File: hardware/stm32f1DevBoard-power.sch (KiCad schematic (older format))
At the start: 17 parts, among them J2 POWER_JACK, Q1 MOSFET-N, U3 LM358, U4 VREG_GNDCENTER, U5 VREG_VOUTCENTER

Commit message: more mods
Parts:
- added unit 2 of U3
- D2: value POWER -> POWERLED
- JP8: value JUMPER_3X1 -> BATTERYENABLE
- U4: value VREG_GNDCENTER -> VREG-X-5
- U5: value VREG_VOUTCENTER -> VREG-5-3.3
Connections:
- wire segments 55 -> 62
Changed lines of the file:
@@
-EESchema Schematic File Version 2  date Sun 16 Dec 2012 03:06:52 PM EST
+EESchema Schematic File Version 2  date Sun 16 Dec 2012 11:20:27 PM EST
 LIBS:stm32f1DevBoard
 LIBS:power
@@
 Sheet 3 4
 Title ""
-Date "16 dec 2012"
+Date "17 dec 2012"
 Rev ""
 Comp ""
@@
 P 3250 1450
 F 0 "JP8" H 3200 1600 60  0000 C CNN
-F 1 "JUMPER_3X1" H 3250 1250 60  0000 C CNN
+F 1 "BATTERYENABLE" H 3250 1250 60  0000 C CNN
 	1    3250 1450
 	1    0    0    -1
@@
 L MOSFET-N Q1
 U 1 1 50CE2C67
-P 4150 6150
-F 0 "Q1" H 4200 6300 60  0000 C CNN
-F 1 "MOSFET-N" H 4400 6000 60  0000 C CNN
-	1    4150 6150
+P 5650 6250
+F 0 "Q1" H 5700 6400 60  0000 C CNN
+F 1 "MOSFET-N" H 5900 6100 60  0000 C CNN
+	1    5650 6250
 	1    0    0    -1
 $EndComp
@@
 L +5V #PWR048
 U 1 1 50CE2C6E
-P 4400 6150
-F 0 "#PWR048" H 4400 6240 20  0001 C CNN
-F 1 "+5V" H 4400 6240 30  0000 C CNN
-	1    4400 6150
+P 5900 6250
+F 0 "#PWR048" H 5900 6340 20  0001 C CNN
+F 1 "+5V" H 5900 6340 30  0000 C CNN
+	1    5900 6250
 	1    0    0    -1
 $EndComp
@@
 P 3700 3700
 F 0 "U4" H 3850 3504 60  0000 C CNN
-F 1 "VREG_GNDCENTER" H 3700 3900 60  0000 C CNN
+F 1 "VREG-X-5" H 3700 3900 60  0000 C CNN
 	1    3700 3700
 	1    0    0    -1
@@
 P 8150 3800
 F 0 "U5" H 8300 3604 60  0000 C CNN
-F 1 "VREG_VOUTCENTER" H 8150 4000 60  0000 C CNN
+F 1 "VREG-5-3.3" H 8150 4000 60  0000 C CNN
 	1    8150 3800
 	1    0    0    -1
@@
 	3200 5700 3200 5750
 Wire Wire Line
-	3800 6150 3900 6150
-Wire Wire Line
-	4100 5950 4100 5750
-Wire Wire Line
-	4100 5750 4000 5750
-Wire Wire Line
-	4400 6150 4400 6450
-Wire Wire Line
-	4100 6450 4100 6350
+	5600 6050 5600 5850
+Wire Wire Line
+	5600 5850 5500 5850
+Wire Wire Line
+	5900 6250 5900 6550
+Wire Wire Line
+	5600 6550 5600 6450
 Wire Wire Line
 	8150 4050 8150 4100
 Wire Wire Line
-	4400 6450 4100 6450
+	5900 6550 5600 6550
 Wire Wire Line
 	8550 3750 8850 3750
@@
 P 8550 1600
 F 0 "D2" H 8550 1700 50  0000 C CNN
-F 1 "POWER" H 8550 1500 50  0000 C CNN
+F 1 "POWERLED" H 8550 1500 50  0000 C CNN
 	1    8550 1600
 	1    0    0    -1
@@
 Text GLabel 3650 1450 2    60   Input ~ 0
 VBAT
-Text GLabel 4000 5750 0    60   Input ~ 0
+Text GLabel 5500 5850 0    60   Input ~ 0
 VUSB
 Text GLabel 2200 5500 0    60   Input ~ 0
@@
 Text GLabel 3250 3650 0    60   Input ~ 0
 VIN
+$Comp
+L LM358 U3
+U 2 1 50CE9E50
+P 4500 6250
+F 0 "U3" H 4450 6450 60  0000 L CNN
+F 1 "LM358" H 4450 6000 60  0000 L CNN
+	2    4500 6250
+	1    0    0    -1
+$EndComp
+Wire Wire Line
+	3800 6150 4000 6150
+Wire Wire Line
+	5000 6250 5400 6250
+Wire Wire Line
+	5100 6250 5100 6850
+Wire Wire Line
+	5100 6850 3900 6850
+Wire Wire Line
+	3900 6850 3900 6350
+Wire Wire Line
+	3900 6350 4000 6350
+Connection ~ 5100 6250
+$Comp
+L GND #PWR?
+U 1 1 50CEA124
+P 4400 6700
+F 0 "#PWR?" H 4400 6700 30  0001 C CNN
+F 1 "GND" H 4400 6630 30  0001 C CNN
+	1    4400 6700
+	1    0    0    -1
+$EndComp
+$Comp
+L +5V #PWR?
+U 1 1 50CEA12A
+P 4400 5800
+F 0 "#PWR?" H 4400 5890 20  0001 C CNN
+F 1 "+5V" H 4400 5890 30  0000 C CNN
+	1    4400 5800
+	1    0    0    -1
+$EndComp
+Wire Wire Line
+	4400 6650 4400 6700
+Wire Wire Line
+	4400 5800 4400 5850
 $EndSCHEMATC

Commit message: changed to p-ch mosfet
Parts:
- removed Q1: MOSFET-N, symbol MOSFET-N
- added Q1: MOSFET-P, symbol MOSFET-P
- R14: value ? -> 68k
- R15: value ? -> 33k
- R16, R17: value ? -> 100k
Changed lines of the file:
@@
-EESchema Schematic File Version 2  date Wed 19 Dec 2012 08:51:07 PM EST
+EESchema Schematic File Version 2  date Wed 19 Dec 2012 11:05:56 PM EST
 LIBS:stm32f1DevBoard
 LIBS:power
@@
 Sheet 3 4
 Title ""
-Date "19 dec 2012"
+Date "20 dec 2012"
 Rev ""
 Comp ""
@@
 $EndComp
 $Comp
-L GND #PWR38
+L GND #PWR038
 U 1 1 50CE2BF2
 P 2100 1800
-F 0 "#PWR38" H 2100 1800 30  0001 C CNN
+F 0 "#PWR038" H 2100 1800 30  0001 C CNN
 F 1 "GND" H 2100 1730 30  0001 C CNN
 	1    2100 1800
@@
 $EndComp
 $Comp
-L +3.3V #PWR42
+L +3.3V #PWR039
 U 1 1 50CE2BF8
 P 2900 1300
-F 0 "#PWR42" H 2900 1260 30  0001 C CNN
+F 0 "#PWR039" H 2900 1260 30  0001 C CNN
 F 1 "+3.3V" H 2900 1410 30  0000 C CNN
 	1    2900 1300
@@
 $EndComp
 $Comp
-L GND #PWR40
+L GND #PWR040
 U 1 1 50CE2C12
 P 2600 3950
-F 0 "#PWR40" H 2600 3950 30  0001 C CNN
+F 0 "#PWR040" H 2600 3950 30  0001 C CNN
 F 1 "GND" H 2600 3880 30  0001 C CNN
 	1    2600 3950
@@
 $EndComp
 $Comp
-L GND #PWR45
+L GND #PWR041
 U 1 1 50CE2C18
 P 3600 4050
-F 0 "#PWR45" H 3600 4050 30  0001 C CNN
+F 0 "#PWR041" H 3600 4050 30  0001 C CNN
 F 1 "GND" H 3600 3980 30  0001 C CNN
 	1    3600 4050
@@
 $EndComp
 $Comp
-L +5V #PWR49
+L +5V #PWR042
 U 1 1 50CE2C1E
 P 4500 3550
-F 0 "#PWR49" H 4500 3640 20  0001 C CNN
+F 0 "#PWR042" H 4500 3640 20  0001 C CNN
 F 1 "+5V" H 4500 3640 30  0000 C CNN
 	1    4500 3550
@@
 $EndComp
 $Comp
-L GND #PWR46
+L GND #PWR043
 U 1 1 50CE2C2A
 P 4200 4050
-F 0 "#PWR46" H 4200 4050 30  0001 C CNN
+F 0 "#PWR043" H 4200 4050 30  0001 C CNN
 F 1 "GND" H 4200 3980 30  0001 C CNN
 	1    4200 4050
@@
 P 2700 5800
 F 0 "R16" H 2710 5890 60  0000 C CNN
-F 1 "?" H 2710 5700 60  0000 C CNN
+F 1 "100k" H 2710 5700 60  0000 C CNN
 	1    2700 5800
 	0    -1   -1   0
@@
 P 2700 6550
 F 0 "R17" H 2710 6640 60  0000 C CNN
-F 1 "?" H 2710 6450 60  0000 C CNN
+F 1 "100k" H 2710 6450 60  0000 C CNN
 	1    2700 6550
 	0    -1   -1   0
@@
 P 2400 5800
 F 0 "R14" H 2410 5890 60  0000 C CNN
-F 1 "?" H 2410 5700 60  0000 C CNN
+F 1 "68k" H 2410 5700 60  0000 C CNN
 	1    2400 5800
 	0    -1   -1   0
@@
 P 2400 6550
 F 0 "R15" H 2410 6640 60  0000 C CNN
-F 1 "?" H 2410 6450 60  0000 C CNN
+F 1 "33k" H 2410 6450 60  0000 C CNN
 	1    2400 6550
 	0    -1   -1   0
 $EndComp
 $Comp
-L +5V #PWR41
+L +5V #PWR044
 U 1 1 50CE2C4E
 P 2700 5550
-F 0 "#PWR41" H 2700 5640 20  0001 C CNN
+F 0 "#PWR044" H 2700 5640 20  0001 C CNN
 F 1 "+5V" H 2700 5640 30  0000 C CNN
 	1    2700 5550
@@
 $EndComp
 $Comp
-L GND #PWR39
+L GND #PWR045
 U 1 1 50CE2C55
 P 2400 6800
-F 0 "#PWR39" H 2400 6800 30  0001 C CNN
+F 0 "#PWR045" H 2400 6800 30  0001 C CNN
 F 1 "GND" H 2400 6730 30  0001 C CNN
 	1    2400 6800
@@
 $EndComp
 $Comp
-L GND #PWR44
+L GND #PWR046
 U 1 1 50CE2C5B
 P 3200 6600
-F 0 "#PWR44" H 3200 6600 30  0001 C CNN
+F 0 "#PWR046" H 3200 6600 30  0001 C CNN
 F 1 "GND" H 3200 6530 30  0001 C CNN
 	1    3200 6600
@@
 $EndComp
 $Comp
-L +5V #PWR43
+L +5V #PWR047
 U 1 1 50CE2C61
 P 3200 5700
-F 0 "#PWR43" H 3200 5790 20  0001 C CNN
+F 0 "#PWR047" H 3200 5790 20  0001 C CNN
 F 1 "+5V" H 3200 5790 30  0000 C CNN
 	1    3200 5700
@@
 $EndComp
 $Comp
-L MOSFET-N Q1
-U 1 1 50CE2C67
-P 5650 6250
-F 0 "Q1" H 5700 6400 60  0000 C CNN
-F 1 "MOSFET-N" H 5900 6100 60  0000 C CNN
-	1    5650 6250
-	1    0    0    -1
-$EndComp
-$Comp
-L +5V #PWR50
+L +5V #PWR048
 U 1 1 50CE2C6E
 P 5900 6250
-F 0 "#PWR50" H 5900 6340 20  0001 C CNN
+F 0 "#PWR048" H 5900 6340 20  0001 C CNN
 F 1 "+5V" H 5900 6340 30  0000 C CNN
 	1    5900 6250
@@
 $EndComp
 $Comp
-L GND #PWR53
+L GND #PWR049
 U 1 1 50CE2C74
 P 8150 4100
-F 0 "#PWR53" H 8150 4100 30  0001 C CNN
+F 0 "#PWR049" H 8150 4100 30  0001 C CNN
 F 1 "GND" H 8150 4030 30  0001 C CNN
 	1    8150 4100
@@
 $EndComp
 $Comp
-L +3.3V #PWR56
+L +3.3V #PWR050
 U 1 1 50CE2C7A
 P 8850 3650
-F 0 "#PWR56" H 8850 3610 30  0001 C CNN
+F 0 "#PWR050" H 8850 3610 30  0001 C CNN
 F 1 "+3.3V" H 8850 3760 30  0000 C CNN
 	1    8850 3650
@@
 $EndComp
 $Comp
-L GND #PWR54
+L GND #PWR051
 U 1 1 50CE2C86
 P 8750 4200
-F 0 "#PWR54" H 8750 4200 30  0001 C CNN
+F 0 "#PWR051" H 8750 4200 30  0001 C CNN
 F 1 "GND" H 8750 4130 30  0001 C CNN
 	1    8750 4200
@@
 $EndComp
 $Comp
-L +5V #PWR51
+L +5V #PWR052
 U 1 1 50CE2C8C
 P 7650 3600
-F 0 "#PWR51" H 7650 3690 20  0001 C CNN
+F 0 "#PWR052" H 7650 3690 20  0001 C CNN
 F 1 "+5V" H 7650 3690 30  0000 C CNN
 	1    7650 3600
@@
 $EndComp
 $Comp
-L GND #PWR55
+L GND #PWR053
 U 1 1 50CE2CF6
 P 8850 1700
-F 0 "#PWR55" H 8850 1700 30  0001 C CNN
+F 0 "#PWR053" H 8850 1700 30  0001 C CNN
 F 1 "GND" H 8850 1630 30  0001 C CNN
 	1    8850 1700
@@
 	8350 1600 8200 1600
 $Comp
-L +3.3V #PWR52
+L +3.3V #PWR054
 U 1 1 50CE2CFF
 P 7750 1500
-F 0 "#PWR52" H 7750 1460 30  0001 C CNN
+F 0 "#PWR054" H 7750 1460 30  0001 C CNN
 F 1 "+3.3V" H 7750 1610 30  0000 C CNN
 	1    7750 1500
@@
 Connection ~ 5100 6250
 $Comp
-L GND #PWR48
+L GND #PWR055
 U 1 1 50CEA124
 P 4400 6700
-F 0 "#PWR48" H 4400 6700 30  0001 C CNN
+F 0 "#PWR055" H 4400 6700 30  0001 C CNN
 F 1 "GND" H 4400 6630 30  0001 C CNN
 	1    4400 6700
@@
 $EndComp
 $Comp
-L +5V #PWR47
+L +5V #PWR056
 U 1 1 50CEA12A
 P 4400 5800
-F 0 "#PWR47" H 4400 5890 20  0001 C CNN
+F 0 "#PWR056" H 4400 5890 20  0001 C CNN
 F 1 "+5V" H 4400 5890 30  0000 C CNN
 	1    4400 5800
@@
 Wire Wire Line
 	4400 5800 4400 5850
+$Comp
+L MOSFET-P Q1
+U 1 1 50D29082
+P 5650 6250
+F 0 "Q1" H 5700 6400 60  0000 C CNN
+F 1 "MOSFET-P" H 5900 6100 60  0000 C CNN
+	1    5650 6250
+	1    0    0    -1
+$EndComp
 $EndSCHEMATC

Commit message: using kicadcloud files
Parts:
- C15, C16: symbol CSMALL -> CPsmall
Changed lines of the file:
@@
-EESchema Schematic File Version 2  date Wed 19 Dec 2012 11:05:56 PM EST
-LIBS:stm32f1DevBoard
+EESchema Schematic File Version 2  date Wed 02 Jan 2013 12:15:05 PM EST
+LIBS:userFavorites
 LIBS:power
-LIBS:device
-LIBS:transistors
-LIBS:conn
-LIBS:linear
-LIBS:regul
-LIBS:74xx
-LIBS:cmos4000
-LIBS:adc-dac
-LIBS:memory
-LIBS:xilinx
-LIBS:special
-LIBS:microcontrollers
-LIBS:dsp
-LIBS:microchip
-LIBS:analog_switches
-LIBS:motorola
-LIBS:texas
-LIBS:intel
-LIBS:audio
-LIBS:interface
-LIBS:digital-audio
-LIBS:philips
-LIBS:display
-LIBS:cypress
-LIBS:siliconi
-LIBS:opto
-LIBS:atmel
-LIBS:contrib
-LIBS:valves
-LIBS:stm32f1DevBoard-cache
 EELAYER 27 0
 EELAYER END
@@
 $EndComp
 $Comp
-L CSMALL C15
+L CPsmall C15
 U 1 1 50CE2C24
 P 4400 3850
@@
 $EndComp
 $Comp
-L CSMALL C16
+L CPsmall C16
 U 1 1 50CE2C80
 P 8750 4050

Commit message: updates to schematic
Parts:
- R18: value ? -> 100
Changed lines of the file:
@@
-EESchema Schematic File Version 2  date Thu 17 Jan 2013 09:41:47 PM EST
+EESchema Schematic File Version 2  date Mon 21 Jan 2013 10:28:50 PM EST
 LIBS:userFavorites
 LIBS:power
+LIBS:stm32f1DevBoard-cache
 EELAYER 27 0
 EELAYER END
@@
 Sheet 3 4
 Title ""
-Date "18 jan 2013"
+Date "22 jan 2013"
 Rev ""
 Comp ""
@@
 P 8000 1600
 F 0 "R18" H 8010 1690 60  0000 C CNN
-F 1 "?" H 8010 1500 60  0000 C CNN
+F 1 "100" H 8010 1500 60  0000 C CNN
 	1    8000 1600
 	1    0    0    -1

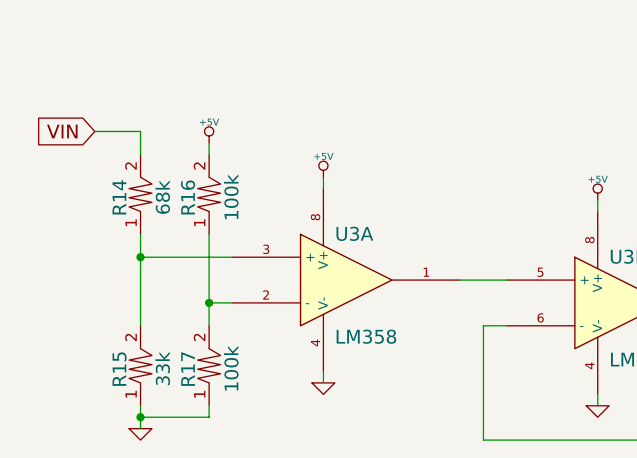
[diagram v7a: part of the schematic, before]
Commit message: fix sdcard
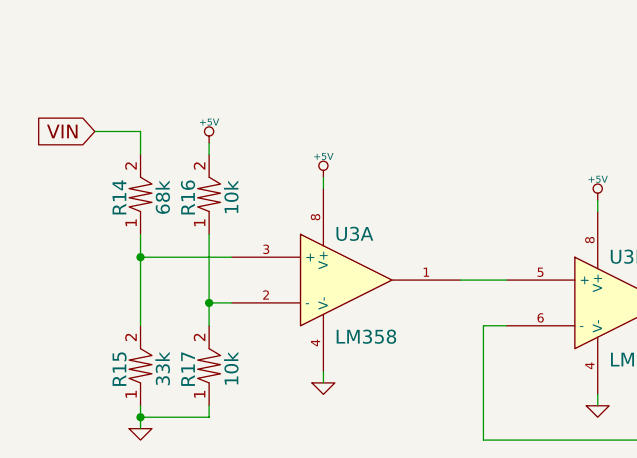
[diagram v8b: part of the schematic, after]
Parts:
- R16, R17: value 100k -> 10k
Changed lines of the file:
@@
-EESchema Schematic File Version 2  date Mon 21 Jan 2013 10:28:50 PM EST
+EESchema Schematic File Version 2  date Tue 29 Jan 2013 12:07:46 AM EST
 LIBS:userFavorites
 LIBS:power
@@
 Sheet 3 4
 Title ""
-Date "22 jan 2013"
+Date "29 jan 2013"
 Rev ""
 Comp ""
@@
 $EndComp
 $Comp
-L GND #PWR38
+L GND #PWR038
 U 1 1 50CE2BF2
 P 2100 1800
-F 0 "#PWR38" H 2100 1800 30  0001 C CNN
+F 0 "#PWR038" H 2100 1800 30  0001 C CNN
 F 1 "GND" H 2100 1730 30  0001 C CNN
 	1    2100 1800
@@
 $EndComp
 $Comp
-L +3.3V #PWR42
+L +3.3V #PWR039
 U 1 1 50CE2BF8
 P 2900 1300
-F 0 "#PWR42" H 2900 1260 30  0001 C CNN
+F 0 "#PWR039" H 2900 1260 30  0001 C CNN
 F 1 "+3.3V" H 2900 1410 30  0000 C CNN
 	1    2900 1300
@@
 $EndComp
 $Comp
-L GND #PWR40
+L GND #PWR040
 U 1 1 50CE2C12
 P 2600 3950
-F 0 "#PWR40" H 2600 3950 30  0001 C CNN
+F 0 "#PWR040" H 2600 3950 30  0001 C CNN
 F 1 "GND" H 2600 3880 30  0001 C CNN
 	1    2600 3950
@@
 $EndComp
 $Comp
-L GND #PWR45
+L GND #PWR041
 U 1 1 50CE2C18
 P 3600 4050
-F 0 "#PWR45" H 3600 4050 30  0001 C CNN
+F 0 "#PWR041" H 3600 4050 30  0001 C CNN
 F 1 "GND" H 3600 3980 30  0001 C CNN
 	1    3600 4050
@@
 $EndComp
 $Comp
-L +5V #PWR49
+L +5V #PWR042
 U 1 1 50CE2C1E
 P 4500 3550
-F 0 "#PWR49" H 4500 3640 20  0001 C CNN
+F 0 "#PWR042" H 4500 3640 20  0001 C CNN
 F 1 "+5V" H 4500 3640 30  0000 C CNN
 	1    4500 3550
@@
 $EndComp
 $Comp
-L GND #PWR46
+L GND #PWR043
 U 1 1 50CE2C2A
 P 4200 4050
-F 0 "#PWR46" H 4200 4050 30  0001 C CNN
+F 0 "#PWR043" H 4200 4050 30  0001 C CNN
 F 1 "GND" H 4200 3980 30  0001 C CNN
 	1    4200 4050
@@
 P 2700 5800
 F 0 "R16" H 2710 5890 60  0000 C CNN
-F 1 "100k" H 2710 5700 60  0000 C CNN
+F 1 "10k" H 2710 5700 60  0000 C CNN
 	1    2700 5800
 	0    -1   -1   0
@@
 P 2700 6550
 F 0 "R17" H 2710 6640 60  0000 C CNN
-F 1 "100k" H 2710 6450 60  0000 C CNN
+F 1 "10k" H 2710 6450 60  0000 C CNN
 	1    2700 6550
 	0    -1   -1   0
@@
 $EndComp
 $Comp
-L +5V #PWR41
+L +5V #PWR044
 U 1 1 50CE2C4E
 P 2700 5550
-F 0 "#PWR41" H 2700 5640 20  0001 C CNN
+F 0 "#PWR044" H 2700 5640 20  0001 C CNN
 F 1 "+5V" H 2700 5640 30  0000 C CNN
 	1    2700 5550
@@
 $EndComp
 $Comp
-L GND #PWR39
+L GND #PWR045
 U 1 1 50CE2C55
 P 2400 6800
-F 0 "#PWR39" H 2400 6800 30  0001 C CNN
+F 0 "#PWR045" H 2400 6800 30  0001 C CNN
 F 1 "GND" H 2400 6730 30  0001 C CNN
 	1    2400 6800
@@
 $EndComp
 $Comp
-L GND #PWR44
+L GND #PWR046
 U 1 1 50CE2C5B
 P 3200 6600
-F 0 "#PWR44" H 3200 6600 30  0001 C CNN
+F 0 "#PWR046" H 3200 6600 30  0001 C CNN
 F 1 "GND" H 3200 6530 30  0001 C CNN
 	1    3200 6600
@@
 $EndComp
 $Comp
-L +5V #PWR43
+L +5V #PWR047
 U 1 1 50CE2C61
 P 3200 5700
-F 0 "#PWR43" H 3200 5790 20  0001 C CNN
+F 0 "#PWR047" H 3200 5790 20  0001 C CNN
 F 1 "+5V" H 3200 5790 30  0000 C CNN
 	1    3200 5700
@@
 $EndComp
 $Comp
-L +5V #PWR50
+L +5V #PWR048
 U 1 1 50CE2C6E
 P 5900 6250
-F 0 "#PWR50" H 5900 6340 20  0001 C CNN
+F 0 "#PWR048" H 5900 6340 20  0001 C CNN
 F 1 "+5V" H 5900 6340 30  0000 C CNN
 	1    5900 6250
@@
 $EndComp
 $Comp
-L GND #PWR53
+L GND #PWR049
 U 1 1 50CE2C74
 P 8150 4100
-F 0 "#PWR53" H 8150 4100 30  0001 C CNN
+F 0 "#PWR049" H 8150 4100 30  0001 C CNN
 F 1 "GND" H 8150 4030 30  0001 C CNN
 	1    8150 4100
@@
 $EndComp
 $Comp
-L +3.3V #PWR56
+L +3.3V #PWR050
 U 1 1 50CE2C7A
 P 8850 3650
-F 0 "#PWR56" H 8850 3610 30  0001 C CNN
+F 0 "#PWR050" H 8850 3610 30  0001 C CNN
 F 1 "+3.3V" H 8850 3760 30  0000 C CNN
 	1    8850 3650
@@
 $EndComp
 $Comp
-L GND #PWR54
+L GND #PWR051
 U 1 1 50CE2C86
 P 8750 4200
-F 0 "#PWR54" H 8750 4200 30  0001 C CNN
+F 0 "#PWR051" H 8750 4200 30  0001 C CNN
 F 1 "GND" H 8750 4130 30  0001 C CNN
 	1    8750 4200
@@
 $EndComp
 $Comp
-L +5V #PWR51
+L +5V #PWR052
 U 1 1 50CE2C8C
 P 7650 3600
-F 0 "#PWR51" H 7650 3690 20  0001 C CNN
+F 0 "#PWR052" H 7650 3690 20  0001 C CNN
 F 1 "+5V" H 7650 3690 30  0000 C CNN
 	1    7650 3600
@@
 $EndComp
 $Comp
-L GND #PWR55
+L GND #PWR053
 U 1 1 50CE2CF6
 P 8850 1700
-F 0 "#PWR55" H 8850 1700 30  0001 C CNN
+F 0 "#PWR053" H 8850 1700 30  0001 C CNN
 F 1 "GND" H 8850 1630 30  0001 C CNN
 	1    8850 1700
@@
 	8350 1600 8200 1600
 $Comp
-L +3.3V #PWR52
+L +3.3V #PWR054
 U 1 1 50CE2CFF
 P 7750 1500
-F 0 "#PWR52" H 7750 1460 30  0001 C CNN
+F 0 "#PWR054" H 7750 1460 30  0001 C CNN
 F 1 "+3.3V" H 7750 1610 30  0000 C CNN
 	1    7750 1500
@@
 Connection ~ 5100 6250
 $Comp
-L GND #PWR48
+L GND #PWR055
 U 1 1 50CEA124
 P 4400 6700
-F 0 "#PWR48" H 4400 6700 30  0001 C CNN
+F 0 "#PWR055" H 4400 6700 30  0001 C CNN
 F 1 "GND" H 4400 6630 30  0001 C CNN
 	1    4400 6700
@@
 $EndComp
 $Comp
-L +5V #PWR47
+L +5V #PWR056
 U 1 1 50CEA12A
 P 4400 5800
-F 0 "#PWR47" H 4400 5890 20  0001 C CNN
+F 0 "#PWR056" H 4400 5890 20  0001 C CNN
 F 1 "+5V" H 4400 5890 30  0000 C CNN
 	1    4400 5800
